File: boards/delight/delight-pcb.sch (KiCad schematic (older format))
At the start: 160 parts, among them J1 AVR-ISP-6, SW0 KEYSW, SW1 KEYSW, SW10 KEYSW, SW11 KEYSW, SW12 KEYSW, SW13 KEYSW, SW14 KEYSW, SW15 KEYSW, SW16 KEYSW, SW17 KEYSW, SW18 KEYSW, SW19 KEYSW, SW2 KEYSW, SW20 KEYSW, SW21 KEYSW, SW22 KEYSW, SW23 KEYSW, SW24 KEYSW, SW25 KEYSW, SW26 KEYSW, SW27 KEYSW, SW28 KEYSW, SW29 KEYSW, SW3 KEYSW, SW30 KEYSW, SW31 KEYSW, SW32 KEYSW, SW33 KEYSW, SW34 KEYSW, SW35 KEYSW, SW36 KEYSW, SW37 KEYSW, SW38 KEYSW, SW39 KEYSW, SW4 KEYSW, SW40 KEYSW, SW41 KEYSW, SW42 KEYSW, SW43 KEYSW, SW44 KEYSW, SW46 KEYSW, SW47 KEYSW, SW48 KEYSW, SW49 KEYSW, SW5 KEYSW, SW50 KEYSW, SW51 KEYSW, SW52 KEYSW, SW53 KEYSW, SW54 KEYSW, SW55 KEYSW, SW56 KEYSW, SW57 KEYSW, SW58 KEYSW, SW59 KEYSW, SW6 KEYSW, SW60 KEYSW, SW61 KEYSW, SW62 KEYSW, SW63 KEYSW, SW64 KEYSW, SW65 KEYSW, SW66 KEYSW, SW67 KEYSW, SW68 KEYSW, SW69 KEYSW, SW7 KEYSW, SW8 KEYSW, SW9 KEYSW, U1 ATmega32A-PU, Y1 Crystal

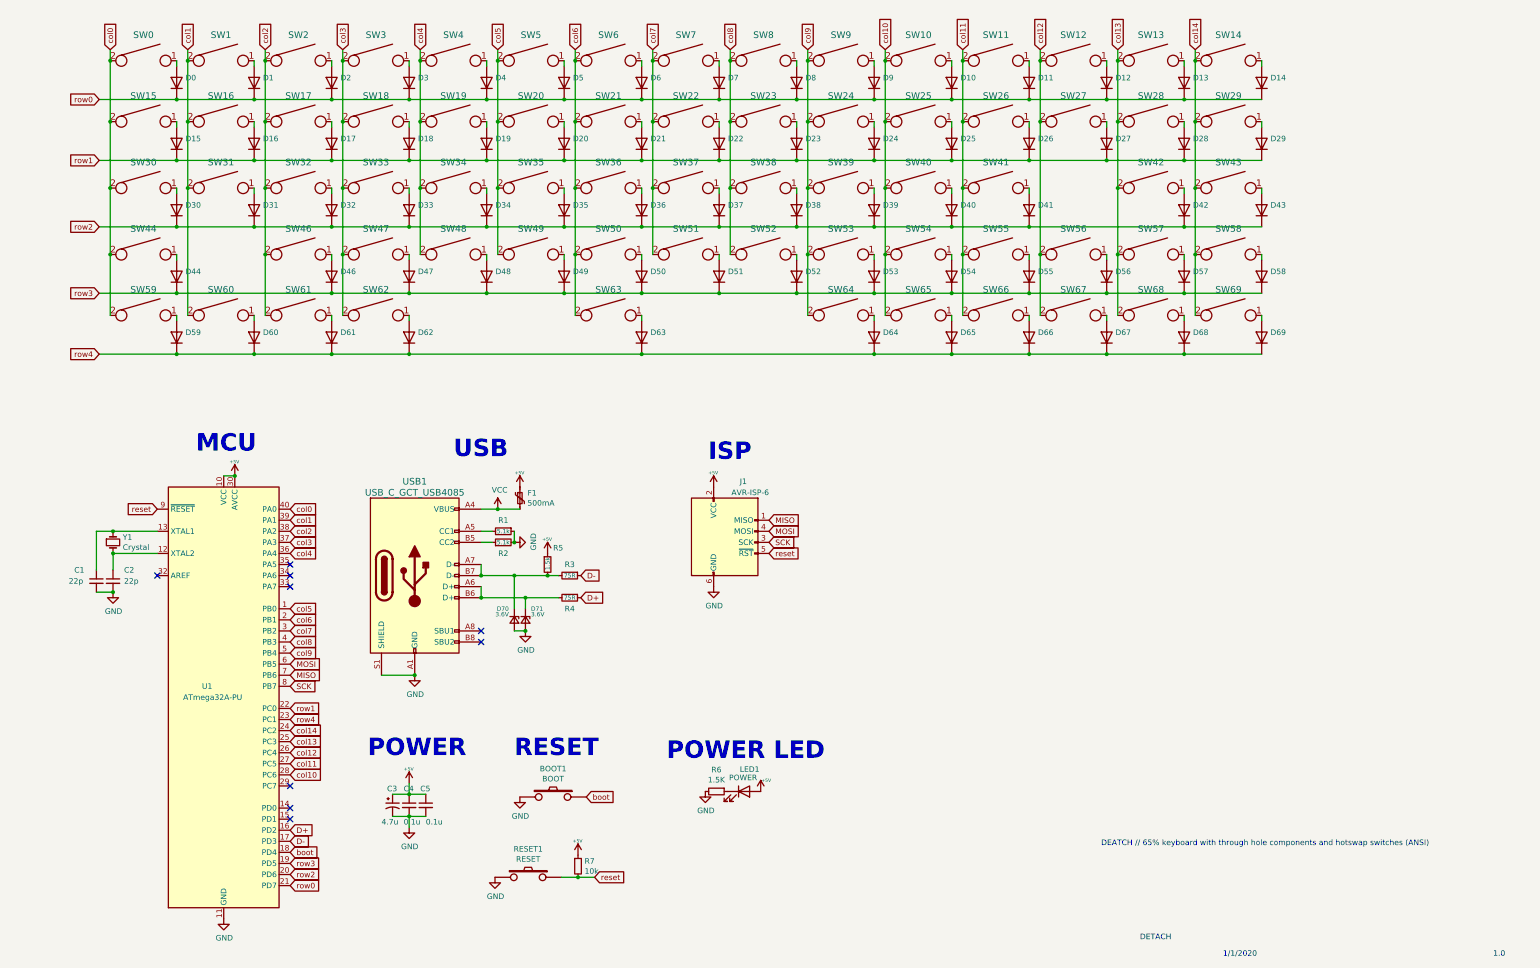
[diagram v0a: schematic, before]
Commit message: Reorg of project layout
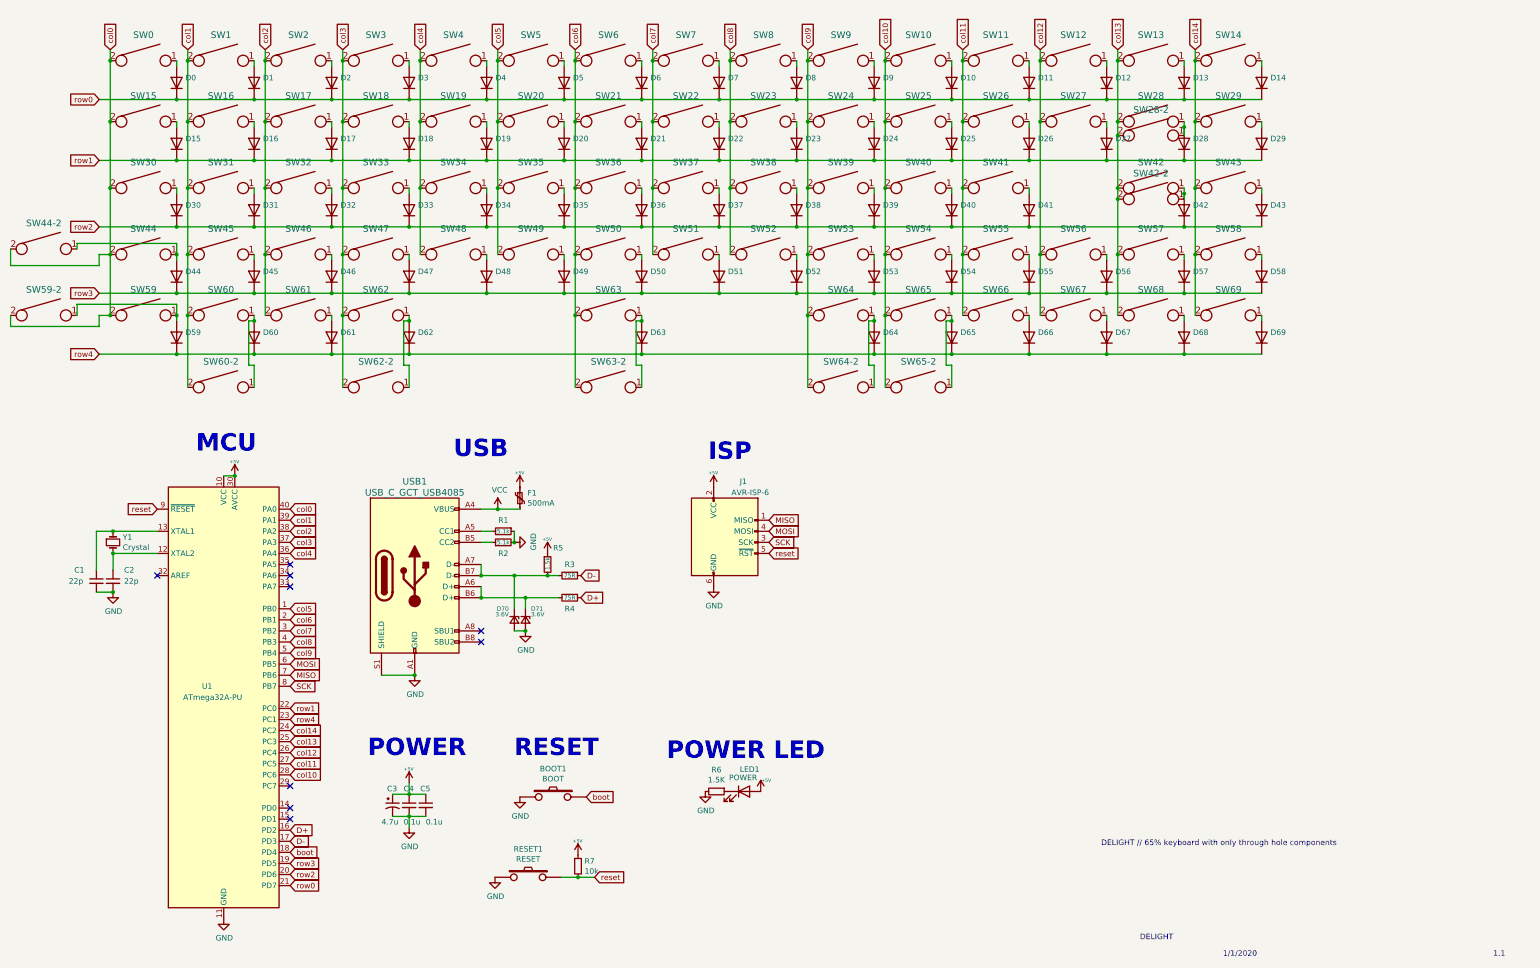
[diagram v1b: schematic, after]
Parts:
- added D45: (no value), Diode_THT:D_DO-35_SOD27_P7.62mm_Horizontal, symbol delight-pcb-rescue:D-Device
- added SW28-2: KEYSW, Switch_Keyboard_Cherry:SW_Cherry_MX_Plate_ISOEnter, symbol delight-pcb-rescue:KEYSW-keyboard_parts
- added SW42-2, SW45: KEYSW, Switch_Keyboard_Cherry:SW_Cherry_MX_PCB_1.00u, symbol delight-pcb-rescue:KEYSW-keyboard_parts
- added SW44-2, SW59-2: KEYSW, Switch_Keyboard_Cherry:SW_Cherry_MX_PCB_1.25u, symbol delight-pcb-rescue:KEYSW-keyboard_parts
- added SW60-2, SW62-2, SW64-2, SW65-2: KEYSW, Switch_Keyboard_Cherry:SW_Cherry_MX_PCB_1.50u, symbol delight-pcb-rescue:KEYSW-keyboard_parts
- added SW63-2: KEYSW, Switch_Keyboard_Cherry:SW_Cherry_MX_PCB_7.00u, symbol delight-pcb-rescue:KEYSW-keyboard_parts
- SW0, SW1, SW10, SW11, SW12, SW14, SW15, SW16, SW17, SW18, SW19, SW2, SW20, SW21, SW22, SW23, SW24, SW25, SW26, SW27, SW29, SW3, SW31, SW32, SW33, SW34, SW35, SW36, SW37, SW38, SW39, SW4, SW40, SW41, SW43, SW46, SW47, SW48, SW49, SW5, SW50, SW51, SW52, SW53, SW54, SW55, SW57, SW58, SW6, SW64, SW65, SW66, SW67, SW68, SW69, SW7, SW8, SW9: footprint Switch_Keyboard_Kailh:SW_Hotswap_Kailh_1.00u -> Switch_Keyboard_Cherry:SW_Cherry_MX_PCB_1.00u
- SW13: footprint Switch_Keyboard_Kailh:SW_Hotswap_Kailh_2.00u -> Switch_Keyboard_Cherry:SW_Cherry_MX_PCB_2.00u
- SW28, SW30: footprint Switch_Keyboard_Kailh:SW_Hotswap_Kailh_1.50u -> Switch_Keyboard_Cherry:SW_Cherry_MX_PCB_1.50u
- SW42, SW59: footprint Switch_Keyboard_Kailh:SW_Hotswap_Kailh_2.25u -> Switch_Keyboard_Cherry:SW_Cherry_MX_PCB_2.25u
- SW44, SW56: footprint Switch_Keyboard_Kailh:SW_Hotswap_Kailh_1.75u -> Switch_Keyboard_Cherry:SW_Cherry_MX_PCB_1.75u
- SW60, SW61, SW62: footprint Switch_Keyboard_Kailh:SW_Hotswap_Kailh_1.25u -> Switch_Keyboard_Cherry:SW_Cherry_MX_PCB_1.25u
- SW63: footprint Switch_Keyboard_Kailh:SW_Hotswap_Kailh_6.25u -> Switch_Keyboard_Cherry:SW_Cherry_MX_PCB_6.25u
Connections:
- net col0: now also SW44-2.2, SW59-2.2
- net col1: now also SW45.2, SW60-2.2
- net col10: now also SW65-2.2
- net col13: now also SW28-2.2, SW42-2.2
- net col3: now also SW62-2.2
- net col6: now also SW63-2.2
- net col9: now also SW64-2.2
- net row3: now also D45.1 (K)
- net at D28.2 (A), SW28.1: now also SW28-2.1
- net at D44.2 (A), SW44.1: now also SW44-2.1
- net at D42.2 (A), SW42.1: now also SW42-2.1
- net at D59.2 (A), SW59.1: now also SW59-2.1
- net at D60.2 (A), SW60.1: now also SW60-2.1
- net at D62.2 (A), SW62.1: now also SW62-2.1
- net at D63.2 (A), SW63.1: now also SW63-2.1
- net at D64.2 (A), SW64.1: now also SW64-2.1
- net at D65.2 (A), SW65.1: now also SW65-2.1
- new net: D45.2 (A), SW45.1
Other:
- note added: "1.1"
- note added: "DELIGHT"
- note added: "DELIGHT // 65% keyboard with only through hole components"
- note removed: "1.0"
- note removed: "DEATCH // 65% keyboard with through hole components and hotswap switches (ANSI)"
- note removed: "DETACH"
